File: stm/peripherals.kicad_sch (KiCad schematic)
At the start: 0 parts

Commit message: PE and PF pin connectors
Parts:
- added J5: Conn_02x16_Odd_Even, symbol Connector_Generic:Conn_02x16_Odd_Even
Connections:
- new net PE0: J5.2 (Pin_2)
- new net PE1: J5.4 (Pin_4)
- new net PE10: J5.22 (Pin_22)
- new net PE11: J5.24 (Pin_24)
- new net PE12: J5.26 (Pin_26)
- new net PE13: J5.28 (Pin_28)
- new net PE14: J5.30 (Pin_30)
- new net PE15: J5.32 (Pin_32)
- new net PE2: J5.6 (Pin_6)
- new net PE3: J5.8 (Pin_8)
- new net PE4: J5.10 (Pin_10)
- new net PE5: J5.12 (Pin_12)
- new net PE6: J5.14 (Pin_14)
- new net PE7: J5.16 (Pin_16)
- new net PE8: J5.18 (Pin_18)
- new net PE9: J5.20 (Pin_20)
- new net PF0: J5.1 (Pin_1)
- new net PF1: J5.3 (Pin_3)
- new net PF10: J5.21 (Pin_21)
- new net PF11: J5.23 (Pin_23)
- new net PF12: J5.25 (Pin_25)
- new net PF13: J5.27 (Pin_27)
- new net PF14: J5.29 (Pin_29)
- new net PF15: J5.31 (Pin_31)
- new net PF2: J5.5 (Pin_5)
- new net PF3: J5.7 (Pin_7)
- new net PF4: J5.9 (Pin_9)
- new net PF5: J5.11 (Pin_11)
- new net PF6: J5.13 (Pin_13)
- new net PF7: J5.15 (Pin_15)
- new net PF8: J5.17 (Pin_17)
- new net PF9: J5.19 (Pin_19)

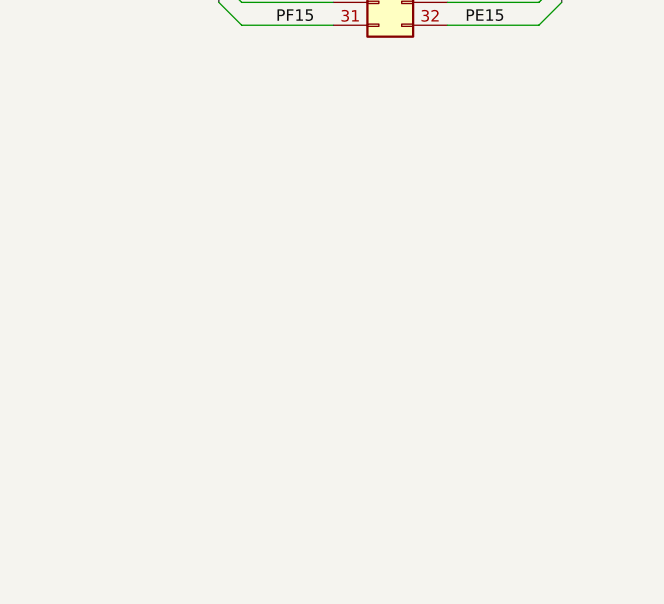
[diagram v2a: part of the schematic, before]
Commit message: added connectors on mcu sheet
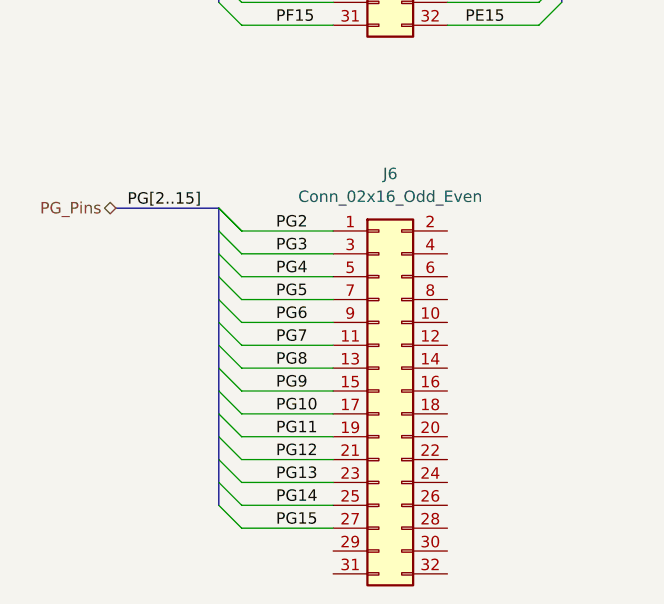
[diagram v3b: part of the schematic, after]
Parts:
- added J6: Conn_02x16_Odd_Even, symbol Connector_Generic:Conn_02x16_Odd_Even
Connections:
- new net PG10: J6.17 (Pin_17)
- new net PG11: J6.19 (Pin_19)
- new net PG12: J6.21 (Pin_21)
- new net PG13: J6.23 (Pin_23)
- new net PG14: J6.25 (Pin_25)
- new net PG15: J6.27 (Pin_27)
- new net PG2: J6.1 (Pin_1)
- new net PG3: J6.3 (Pin_3)
- new net PG4: J6.5 (Pin_5)
- new net PG5: J6.7 (Pin_7)
- new net PG6: J6.9 (Pin_9)
- new net PG7: J6.11 (Pin_11)
- new net PG8: J6.13 (Pin_13)
- new net PG9: J6.15 (Pin_15)

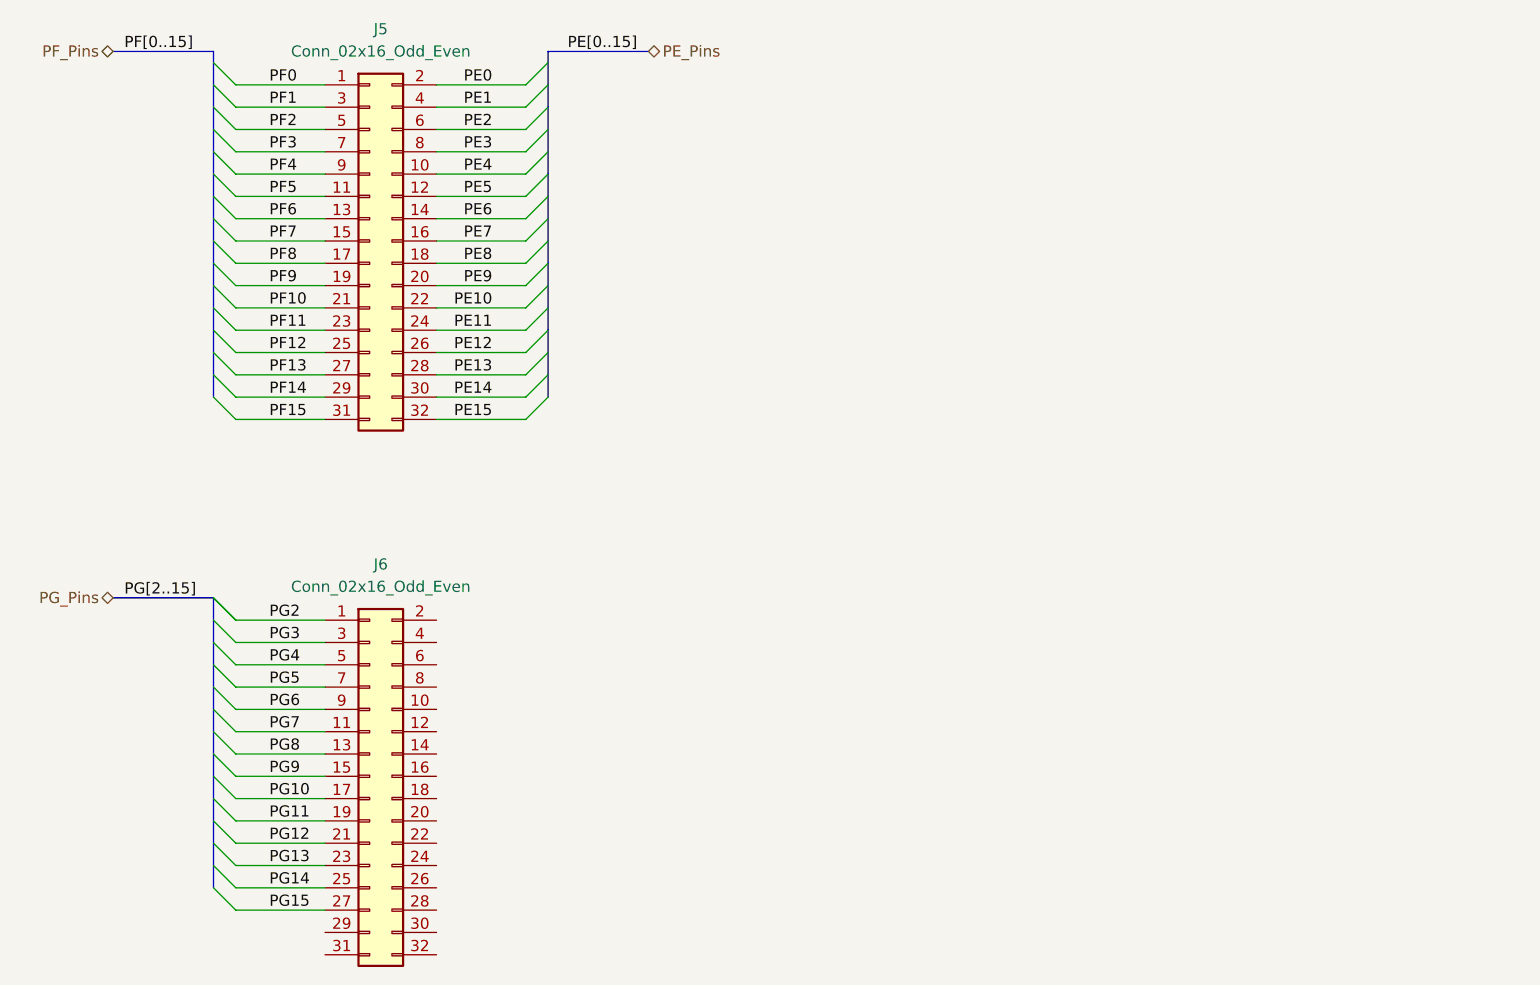
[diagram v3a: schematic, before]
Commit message: completed peripherals mapping
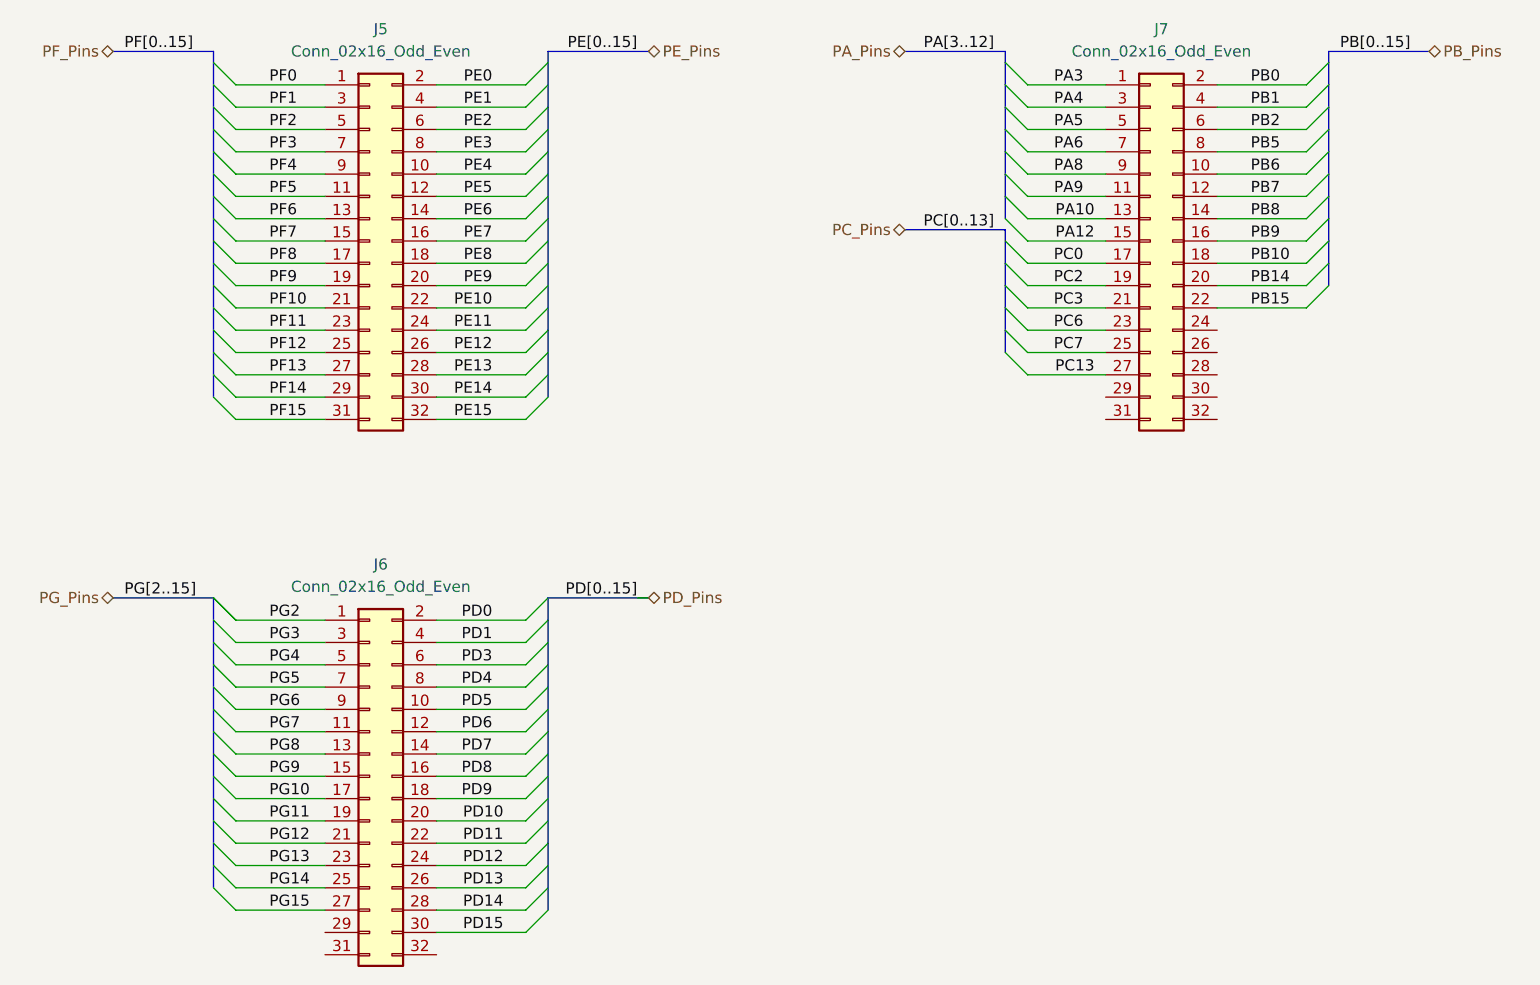
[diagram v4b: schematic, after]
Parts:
- added J7: Conn_02x16_Odd_Even, symbol Connector_Generic:Conn_02x16_Odd_Even
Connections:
- net PD5: now reaches J6.10 (Pin_10)
- net PD6: now reaches J6.12 (Pin_12)
- net PD7: now reaches J6.14 (Pin_14)
- net PD8: now reaches J6.16 (Pin_16)
- net PD9: now reaches J6.18 (Pin_18)
- net PD0: now reaches J6.2 (Pin_2)
- net PD10: now reaches J6.20 (Pin_20)
- net PD11: now reaches J6.22 (Pin_22)
- net PD12: now reaches J6.24 (Pin_24)
- net PD13: now reaches J6.26 (Pin_26)
- net PD14: now reaches J6.28 (Pin_28)
- net PD15: now reaches J6.30 (Pin_30)
- net PD1: now reaches J6.4 (Pin_4)
- net PD3: now reaches J6.6 (Pin_6)
- net PD4: now reaches J6.8 (Pin_8)
- new net PA10: J7.13 (Pin_13)
- new net PA12: J7.15 (Pin_15)
- new net PA3: J7.1 (Pin_1)
- new net PA4: J7.3 (Pin_3)
- new net PA5: J7.5 (Pin_5)
- new net PA6: J7.7 (Pin_7)
- new net PA8: J7.9 (Pin_9)
- new net PA9: J7.11 (Pin_11)
- new net PB0: J7.2 (Pin_2)
- new net PB1: J7.4 (Pin_4)
- new net PB10: J7.18 (Pin_18)
- new net PB14: J7.20 (Pin_20)
- new net PB15: J7.22 (Pin_22)
- new net PB2: J7.6 (Pin_6)
- new net PB5: J7.8 (Pin_8)
- new net PB6: J7.10 (Pin_10)
- new net PB7: J7.12 (Pin_12)
- new net PB8: J7.14 (Pin_14)
- new net PB9: J7.16 (Pin_16)
- new net PC0: J7.17 (Pin_17)
- new net PC13: J7.27 (Pin_27)
- new net PC2: J7.19 (Pin_19)
- new net PC3: J7.21 (Pin_21)
- new net PC6: J7.23 (Pin_23)
- new net PC7: J7.25 (Pin_25)
